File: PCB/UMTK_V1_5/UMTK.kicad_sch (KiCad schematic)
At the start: 10 parts

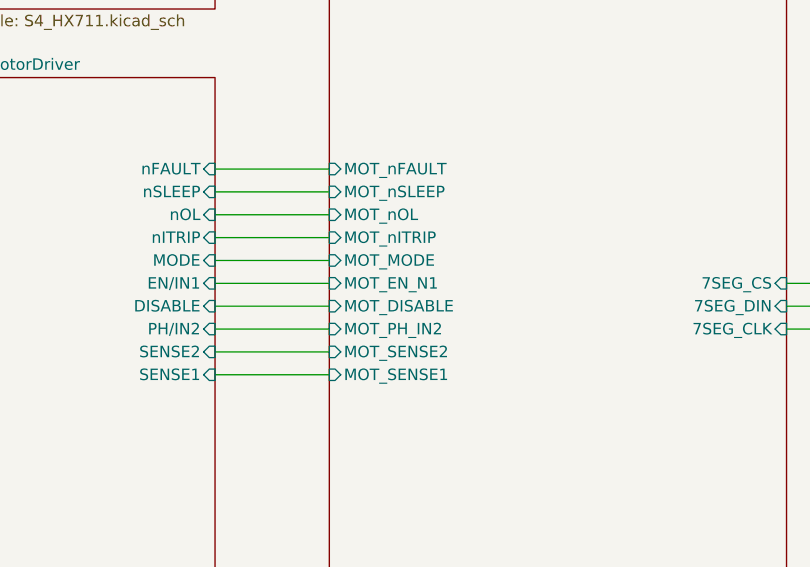
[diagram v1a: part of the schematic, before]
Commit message: Added pin assignment doc for firmware
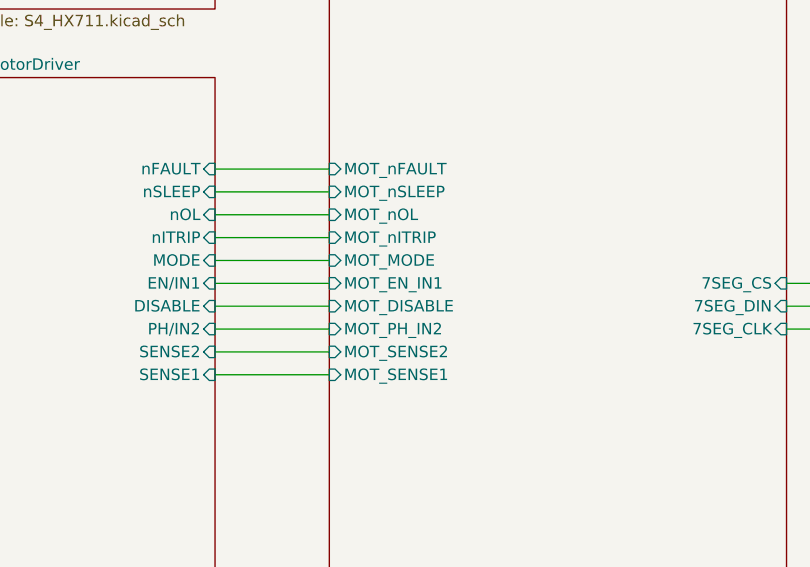
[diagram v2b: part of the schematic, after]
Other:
- sheet Arduino ports: added MOT_EN_IN1; removed MOT_EN_N1
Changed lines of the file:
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@@
-			)
-		)
-		(pin "MOT_EN_N1" input
-			(at 101.6 93.98 180)
-			(effects
-				(font
-					(size 1.27 1.27)
-				)
-				(justify left)
 			)
 		)
@@
 			)
 		)
+		(pin "MOT_EN_IN1" input
+			(at 101.6 93.98 180)
+			(effects
+				(font
+					(size 1.27 1.27)
+				)
+				(justify left)
+			)
+		)
